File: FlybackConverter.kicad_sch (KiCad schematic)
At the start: 32 parts, among them J1 USB_A, T1 Transformer_1P_2S, U1 LNK6448K

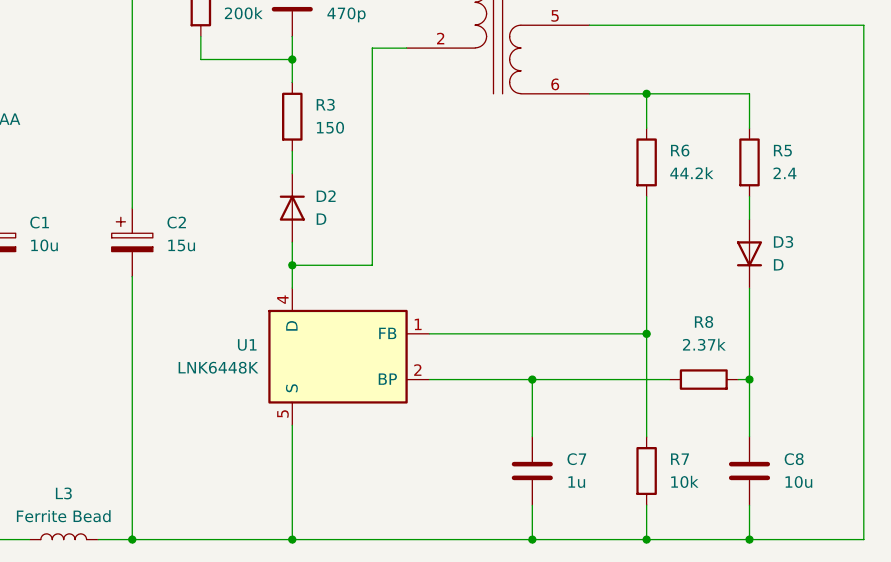
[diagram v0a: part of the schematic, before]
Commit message: スイッチングICをLNK6428Kに変更
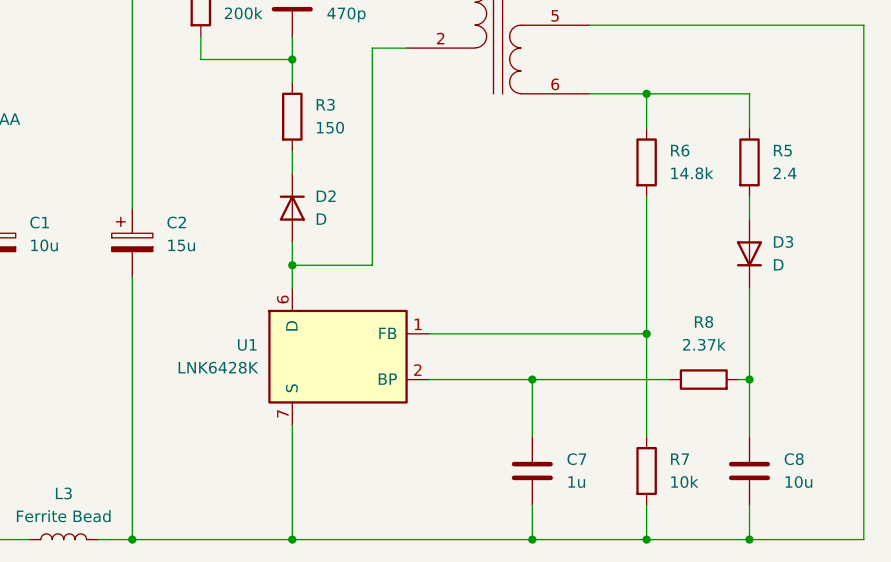
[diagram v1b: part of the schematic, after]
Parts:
- R6: value 44.2k -> 14.8k
- U1: value LNK6448K -> LNK6428K; footprint Package_DIP:PowerIntegrations_PDIP-8C -> Package_SO:PowerIntegrations_eSOP-12B
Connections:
- net at C2.2, C7.2, C8.2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: now also U1.10 (S), U1.11 (S), U1.12 (S), U1.9 (S); no longer U1.5 (S), U1.6 (S)
- net at D2.2 (A), T1.2 (AB): now also U1.6 (D); no longer U1.4 (D)
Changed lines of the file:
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@@
       (effects (font (size 1.27 1.27)) (justify left))
     )
-    (property "Value" "44.2k" (at 168.91 83.82 0)
+    (property "Value" "14.8k" (at 168.91 83.82 0)
       (effects (font (size 1.27 1.27)) (justify left))
     )
@@
       (effects (font (size 1.27 1.27)) (justify right))
     )
-    (property "Value" "LNK6448K" (at 123.19 105.41 0)
+    (property "Value" "LNK6428K" (at 123.19 105.41 0)
       (effects (font (size 1.27 1.27)) (justify right))
     )
-    (property "Footprint" "Package_DIP:PowerIntegrations_PDIP-8C" (at 132.08 104.14 0)
+    (property "Footprint" "Package_SO:PowerIntegrations_eSOP-12B" (at 132.08 104.14 0)
       (effects (font (size 1.27 1.27) italic) hide)
     )
@@
     (pin "1")
     (pin "2")
-    (pin "4")
-    (pin "5")
+    (pin "10")
+    (pin "11")
     (pin "6")
     (pin "7")
     (pin "8")
+    (pin "12")
+    (pin "9")
     (instances
       (project "FlybackConverter"

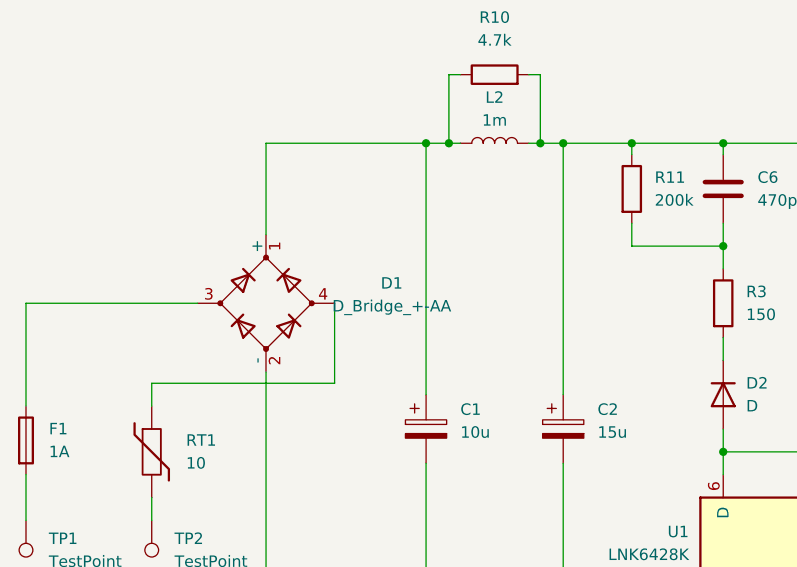
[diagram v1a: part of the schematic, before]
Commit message: フットプリント追加
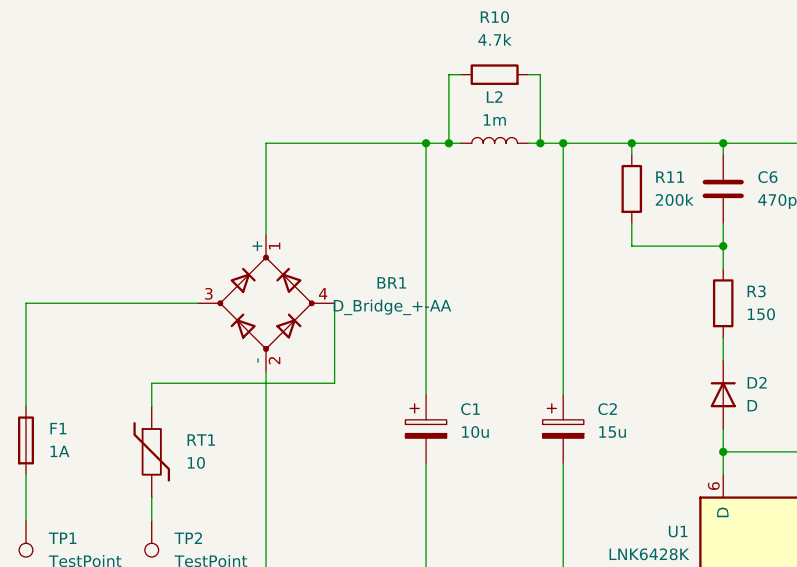
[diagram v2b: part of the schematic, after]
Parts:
- BR1: renamed from D1; footprint (none) -> Package_TO_SOT_SMD:TO-269AA
- C5, C6, C7: footprint (none) -> Capacitor_SMD:C_0805_2012Metric
- C8: footprint (none) -> Capacitor_SMD:C_1206_3216Metric
- D1, D4: footprint (none) -> Diode_SMD:D_PowerDI-5
- D2: footprint (none) -> Diode_SMD:D_SMA
- D3: footprint (none) -> Diode_SMD:D_SMF
- J1: footprint (none) -> Connector_USB:USB_A_CONNFLY_DS1095-WNR0
- L1, L3: footprint (none) -> Resistor_THT:R_Axial_DIN0309_L9.0mm_D3.2mm_P12.70mm_Horizontal
- L2: footprint (none) -> Inductor_THT:L_Radial_D9.5mm_P5.00mm_Fastron_07HVP
- R1, R2: footprint (none) -> Resistor_SMD:R_0805_2012Metric
- R10, R5, R6, R7, R8: footprint (none) -> Resistor_SMD:R_0603_1608Metric
- R11, R3: footprint (none) -> Resistor_SMD:R_1206_3216Metric
- RT1: footprint (none) -> Capacitor_THT:C_Disc_D10.5mm_W5.0mm_P7.50mm

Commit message: フットプリント設定
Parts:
- C1: footprint (none) -> Capacitor_THT:CP_Radial_D10.0mm_P5.00mm
- C2: footprint (none) -> Capacitor_THT:CP_Radial_D12.5mm_P5.00mm
- C3, C4: footprint (none) -> Capacitor_THT:CP_Radial_D8.0mm_P3.50mm
- F1: footprint (none) -> Capacitor_THT:C_Rect_L7.2mm_W4.5mm_P5.00mm_FKS2_FKP2_MKS2_MKP2
- T1: footprint (none) -> Transformer_THT:Transformer_CHK_EI38-3VA_2xSec
- TP1, TP2: footprint (none) -> TestPoint:TestPoint_Loop_D1.80mm_Drill1.0mm_Beaded
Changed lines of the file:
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@@
       (effects (font (size 1.27 1.27)) (justify left))
     )
-    (property "Footprint" "" (at 47.752 92.71 90)
+    (property "Footprint" "Capacitor_THT:C_Rect_L7.2mm_W4.5mm_P5.00mm_FKS2_FKP2_MKS2_MKP2" (at 47.752 92.71 90)
       (effects (font (size 1.27 1.27)) hide)
     )
@@
       (effects (font (size 1.27 1.27)) (justify left))
     )
-    (property "Footprint" "" (at 94.9452 95.25 0)
+    (property "Footprint" "Capacitor_THT:CP_Radial_D10.0mm_P5.00mm" (at 94.9452 95.25 0)
       (effects (font (size 1.27 1.27)) hide)
     )
@@
       (effects (font (size 1.27 1.27)) (justify right))
     )
-    (property "Footprint" "" (at 58.42 101.6 0)
+    (property "Footprint" "TestPoint:TestPoint_Loop_D1.80mm_Drill1.0mm_Beaded" (at 58.42 101.6 0)
       (effects (font (size 1.27 1.27)) hide)
     )
@@
       (effects (font (size 1.27 1.27)) (justify left))
     )
-    (property "Footprint" "" (at 201.6252 60.96 0)
+    (property "Footprint" "Capacitor_THT:CP_Radial_D8.0mm_P3.50mm" (at 201.6252 60.96 0)
       (effects (font (size 1.27 1.27)) hide)
     )
@@
       (effects (font (size 1.27 1.27)) (justify left))
     )
-    (property "Footprint" "" (at 110.1852 95.25 0)
+    (property "Footprint" "Capacitor_THT:CP_Radial_D12.5mm_P5.00mm" (at 110.1852 95.25 0)
       (effects (font (size 1.27 1.27)) hide)
     )
@@
     )
     (pin "1")
-    (pin "2")
     (pin "10")
     (pin "11")
+    (pin "12")
+    (pin "2")
     (pin "6")
     (pin "7")
     (pin "8")
-    (pin "12")
     (pin "9")
     (instances
@@
       (effects (font (size 1.27 1.27)) (justify right))
     )
-    (property "Footprint" "" (at 44.45 101.6 0)
+    (property "Footprint" "TestPoint:TestPoint_Loop_D1.80mm_Drill1.0mm_Beaded" (at 44.45 101.6 0)
       (effects (font (size 1.27 1.27)) hide)
     )
@@
       (effects (font (size 1.27 1.27)))
     )
-    (property "Footprint" "" (at 149.86 64.77 0)
+    (property "Footprint" "Transformer_THT:Transformer_CHK_EI38-3VA_2xSec" (at 149.86 64.77 0)
       (effects (font (size 1.27 1.27)) hide)
     )
@@
       (effects (font (size 1.27 1.27)) (justify left))
     )
-    (property "Footprint" "" (at 216.8652 60.96 0)
-      (effects (font (size 1.27 1.27)) hide)
-    )
+    (property "Footprint" "Capacitor_THT:CP_Radial_D8.0mm_P3.50mm" (at 216.8652 60.96 0)
+      (effects (font (size 1.27 1.27)) hide)
+    )

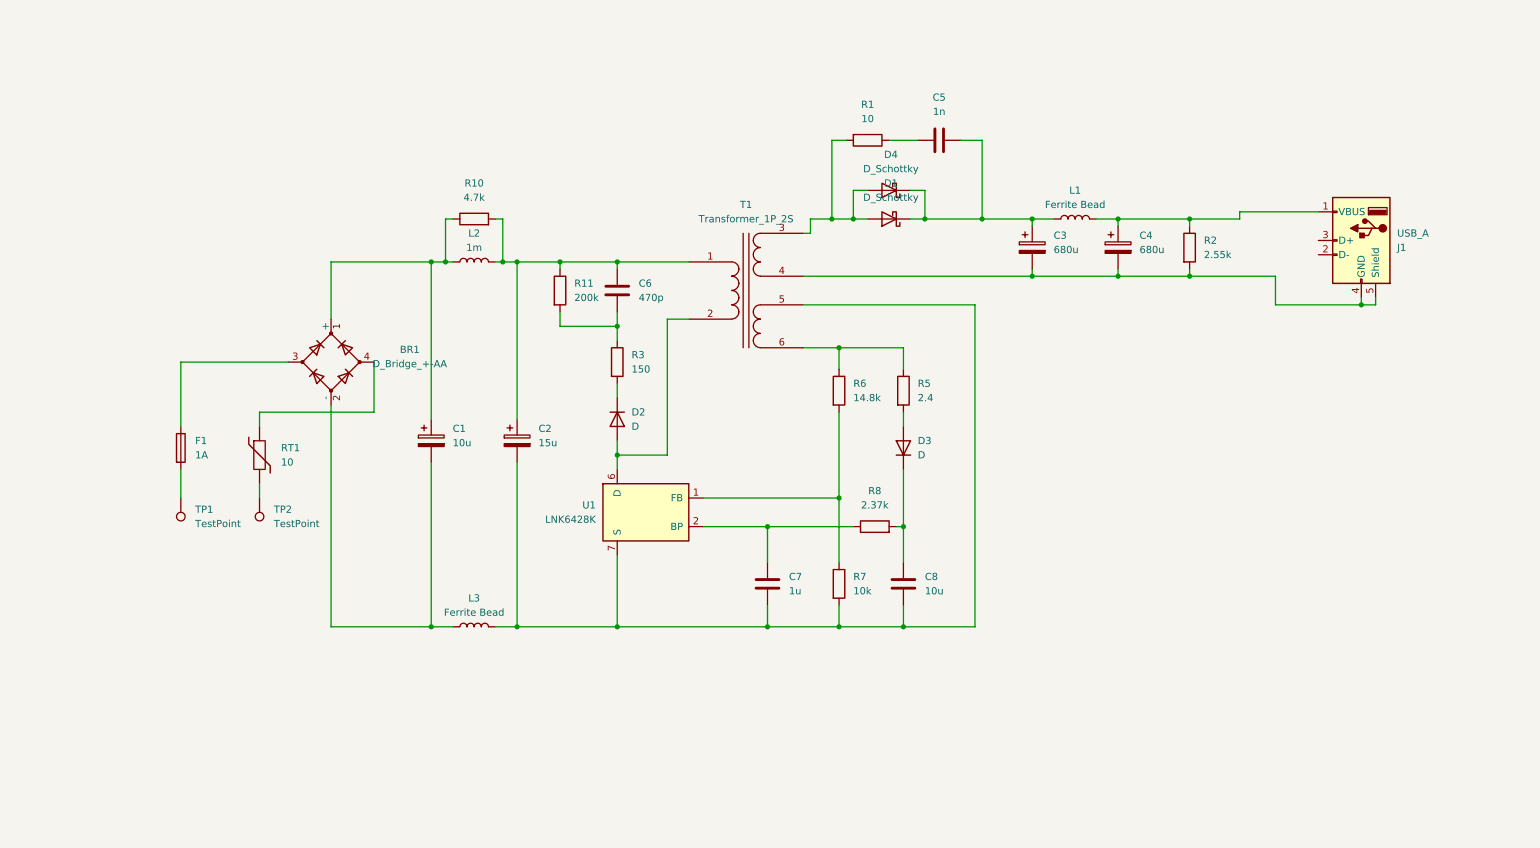
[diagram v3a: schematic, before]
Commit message: トランスのフットプリント修正、FL1,2に合わせてシンボル変更
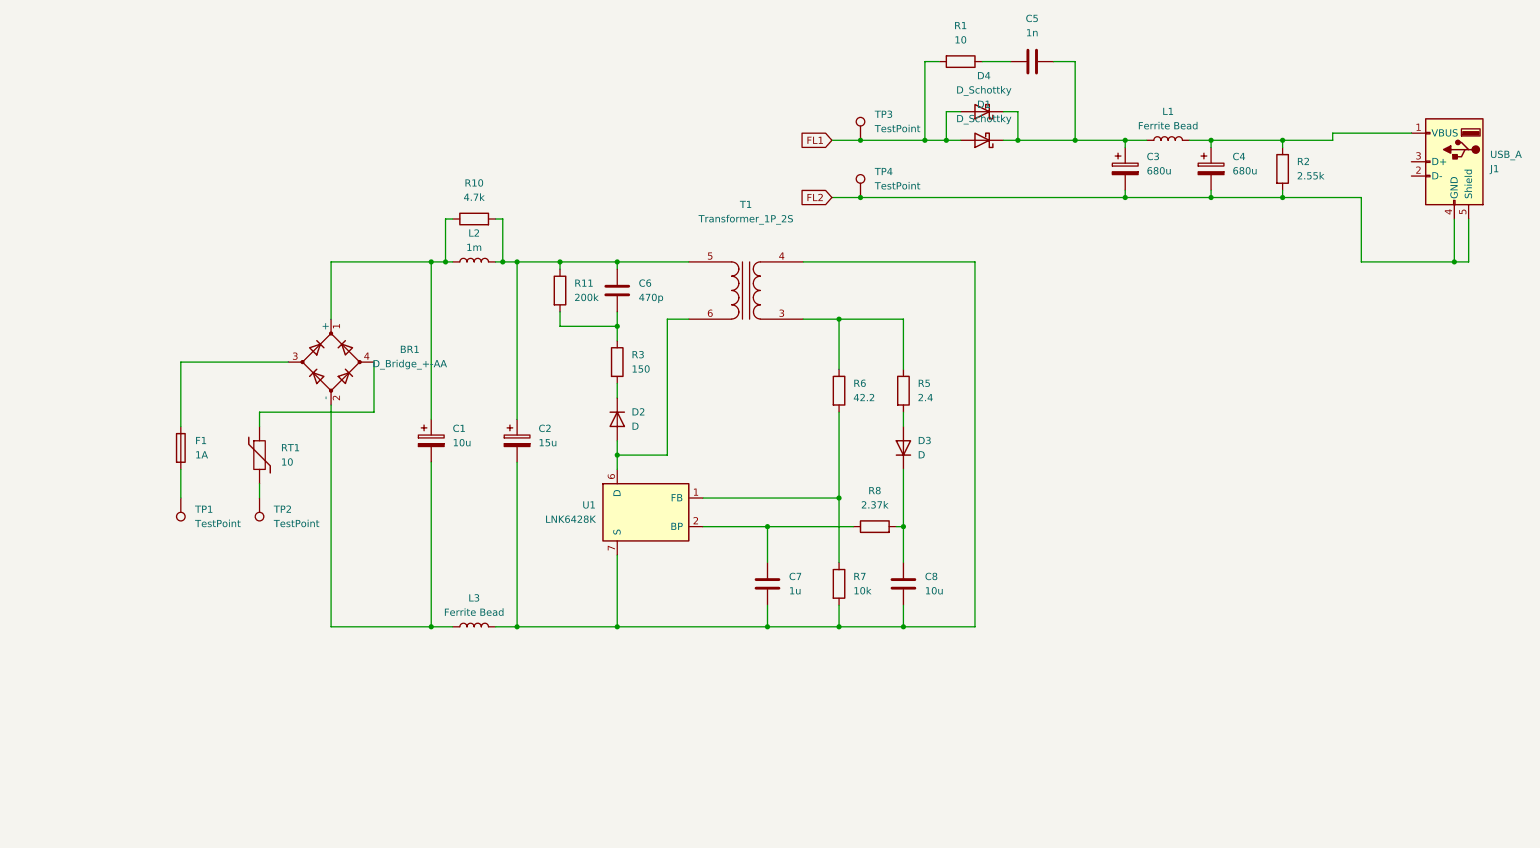
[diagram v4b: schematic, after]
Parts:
- added TP3, TP4: TestPoint, TestPoint:TestPoint_Loop_D1.80mm_Drill1.0mm_Beaded, symbol Connector:TestPoint
- R6: value 14.8k -> 42.2
- T1: symbol Device:Transformer_1P_2S -> Device:Transformer_1P_1S
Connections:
- net at C2.1, C6.1, L2.2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: now also T1.5 (AA); no longer T1.1 (AA)
- net at C2.2, C7.2, C8.2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: now also T1.4 (SB); no longer T1.5 (SC)
- net at D2.2 (A), U1.6 (D): now also T1.6 (AB); no longer T1.2 (AB)
- net FL2: now reaches C3.2, C4.2, J1.4 (GND), J1.5 (Shield), R2.2
- net FL2: now also TP4.1; no longer T1.4 (SB)
- net at R5.1, R6.1: now also T1.3 (SA); no longer T1.6 (SD)
- net FL1: now reaches D1.2 (A), D4.2 (A), R1.2
- net FL1: now also TP3.1; no longer T1.3 (SA)
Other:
- moved on the sheet: C3, C4, C5, D1, D4, J1, L1, R1, R2

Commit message: 仮配置
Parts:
- removed D4: D_Schottky, Diode_SMD:D_PowerDI-5, symbol Device:D_Schottky
- renumbered TP3 to FL1, TP4 to FL2
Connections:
- net at C2.2, C7.2, C8.2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: now also U1.13 (S), U1.3 (S), U1.4 (S)
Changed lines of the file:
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@@
   (junction (at 181.61 38.1) (diameter 0) (color 0 0 0 0)
   )
-  (junction (at 185.42 38.1) (diameter 0) (color 0 0 0 0)
-  )
-  (junction (at 198.12 38.1) (diameter 0) (color 0 0 0 0)
-  )
   (junction (at 109.22 59.69) (diameter 0) (color 0 0 0 0)
   )
@@
     (stroke (width 0) (type default))
   )
-  (wire (pts (xy 198.12 38.1) (xy 208.28 38.1))
+  (wire (pts (xy 195.58 38.1) (xy 208.28 38.1))
     (stroke (width 0) (type default))
   )
@@
     (stroke (width 0) (type default))
   )
-  (wire (pts (xy 185.42 38.1) (xy 187.96 38.1))
-    (stroke (width 0) (type default))
-  )
   (wire (pts (xy 49.53 88.9) (xy 49.53 77.47))
     (stroke (width 0) (type default))
@@
     (stroke (width 0) (type default))
   )
-  (wire (pts (xy 198.12 33.02) (xy 198.12 38.1))
-    (stroke (width 0) (type default))
-  )
   (wire (pts (xy 93.98 59.69) (xy 93.98 87.63))
     (stroke (width 0) (type default))
@@
     (stroke (width 0) (type default))
   )
-  (wire (pts (xy 187.96 33.02) (xy 185.42 33.02))
-    (stroke (width 0) (type default))
-  )
   (wire (pts (xy 245.11 38.1) (xy 245.11 39.37))
     (stroke (width 0) (type default))
@@
     (stroke (width 0) (type default))
   )
-  (wire (pts (xy 185.42 33.02) (xy 185.42 38.1))
-    (stroke (width 0) (type default))
-  )
   (wire (pts (xy 109.22 95.25) (xy 109.22 124.46))
     (stroke (width 0) (type default))
@@
     (stroke (width 0) (type default))
   )
-  (wire (pts (xy 195.58 33.02) (xy 198.12 33.02))
-    (stroke (width 0) (type default))
-  )
   (wire (pts (xy 166.37 101.6) (xy 166.37 86.36))
     (stroke (width 0) (type default))
@@
     (stroke (width 0) (type default))
   )
-  (wire (pts (xy 195.58 38.1) (xy 198.12 38.1))
-    (stroke (width 0) (type default))
-  )
   (wire (pts (xy 83.82 86.36) (xy 83.82 77.47))
     (stroke (width 0) (type default))
@@
     (stroke (width 0) (type default))
   )
-  (wire (pts (xy 181.61 38.1) (xy 185.42 38.1))
+  (wire (pts (xy 181.61 38.1) (xy 187.96 38.1))
     (stroke (width 0) (type default))
   )
@@
     (pin "1")
     (pin "10")
+    (pin "13")
+    (pin "3")
+    (pin "4")
     (pin "11")
     (pin "12")
@@
     )
   )
-  (symbol (lib_id "Device:D_Schottky") (at 191.77 33.02 180) (unit 1)
-    (in_bom yes) (on_board yes) (dnp no) (fields_autoplaced)
-    (property "Reference" "D4" (at 192.0875 26.67 0)
-      (effects (font (size 1.27 1.27)))
-    )
-    (property "Value" "D_Schottky" (at 192.0875 29.21 0)
-      (effects (font (size 1.27 1.27)))
-    )
-    (property "Footprint" "Diode_SMD:D_PowerDI-5" (at 191.77 33.02 0)
-      (effects (font (size 1.27 1.27)) hide)
-    )
-    (property "Datasheet" "~" (at 191.77 33.02 0)
-      (effects (font (size 1.27 1.27)) hide)
-    )
-    (pin "1")
-    (pin "2")
-    (instances
-      (project "FlybackConverter"
-        (path "/f7ad8aa8-e3ae-4e7c-846c-9c0c6caa5ffd"
-          (reference "D4") (unit 1)
-        )
-      )
-    )
-  )
   (symbol (lib_id "Device:C") (at 153.67 116.84 0) (unit 1)
     (in_bom yes) (on_board yes) (dnp no) (fields_autoplaced)
@@
   (symbol (lib_id "Connector:TestPoint") (at 170.18 48.26 0) (unit 1)
     (in_bom yes) (on_board yes) (dnp no) (fields_autoplaced)
-    (property "Reference" "TP4" (at 172.72 43.688 0)
+    (property "Reference" "FL2" (at 172.72 43.688 0)
       (effects (font (size 1.27 1.27)) (justify left))
     )
@@
       (project "FlybackConverter"
         (path "/f7ad8aa8-e3ae-4e7c-846c-9c0c6caa5ffd"
-          (reference "TP4") (unit 1)
+          (reference "FL2") (unit 1)
         )
       )
@@
   (symbol (lib_id "Connector:TestPoint") (at 170.18 38.1 0) (unit 1)
     (in_bom yes) (on_board yes) (dnp no) (fields_autoplaced)
-    (property "Reference" "TP3" (at 172.72 33.528 0)
+    (property "Reference" "FL1" (at 172.72 33.528 0)
       (effects (font (size 1.27 1.27)) (justify left))
     )
@@
       (project "FlybackConverter"
         (path "/f7ad8aa8-e3ae-4e7c-846c-9c0c6caa5ffd"
-          (reference "TP3") (unit 1)
-        )
-      )
+          (reference "FL1") (unit 1)
+        )
+      )

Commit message: TypeC仮配置 #1
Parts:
- removed J1: USB_A, Connector_USB:USB_A_CONNFLY_DS1095-WNR0, symbol Connector:USB_A
- added J1: USB_C_Receptacle_PowerOnly_6P, 00_Library:USB-C-SMD_TYPE-C-6P, symbol Connector:USB_C_Receptacle_PowerOnly_6P
- added R4: 100k, Resistor_SMD:R_0603_1608Metric, symbol Device:R
- added U2: TPS25820DSST, 00_Library:TPS25820, symbol Interface_USB:TPS2513
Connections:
- net FL2: now also J1.A12 (GND), J1.B12 (GND), J1.S1 (SHIELD), R4.2, U2.13 (ThermalPad), U2.3 (GND)
- net 5V: now reaches C4.1, L1.2, R2.1
- net 5V: now also U2.1 (IN), U2.2 (IN)
- new net: J1.B5 (CC2), U2.11 (CC2)
- new net: R4.1, U2.8 (REF)
- new net: J1.A5 (CC1), U2.9 (CC1)
- new net VBUS: J1.A9 (VBUS), J1.B9 (VBUS), U2.12 (OUT)
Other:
- moved on the sheet: BR1, C1, C2, C3, C4, C5, C6, C7, C8, D1, D2, D3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

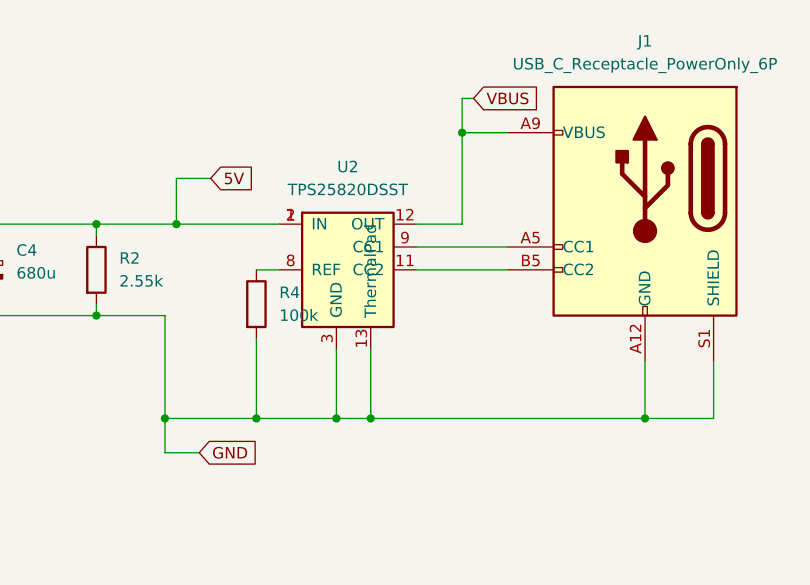
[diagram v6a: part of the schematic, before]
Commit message: USBコントローラ配置 #1
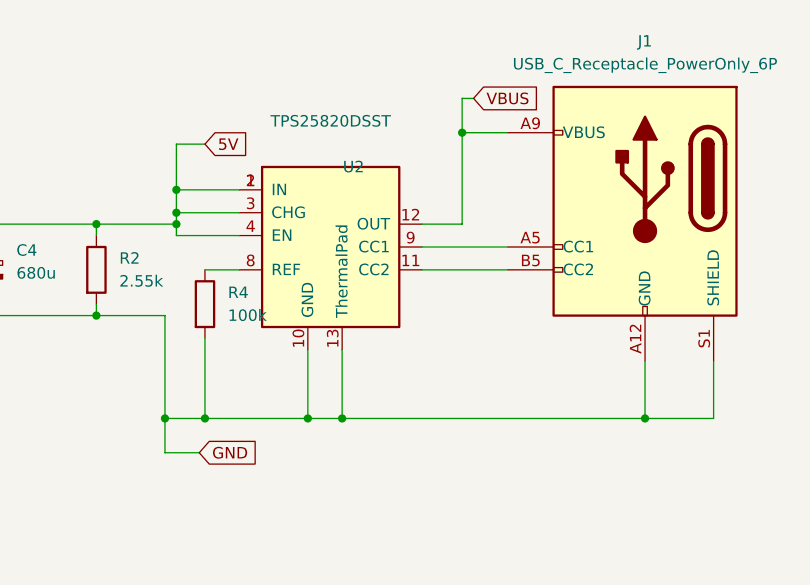
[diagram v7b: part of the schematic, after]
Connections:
- net 5V: now also U2.3 (CHG), U2.4 (EN)
- net FL2: now also U2.10 (GND); no longer U2.3 (GND)
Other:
- moved on the sheet: R4
